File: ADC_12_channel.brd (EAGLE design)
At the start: 160 x 122.4 mm, 165 parts, among them K1 691131710003, K2 691101710002, K3 691101710002, K4 691101710002, K5 691101710002, K6 691101710002, K7 691101710002, K8 691101710002, K9 691101710002, U1 AD7864ASZ-1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

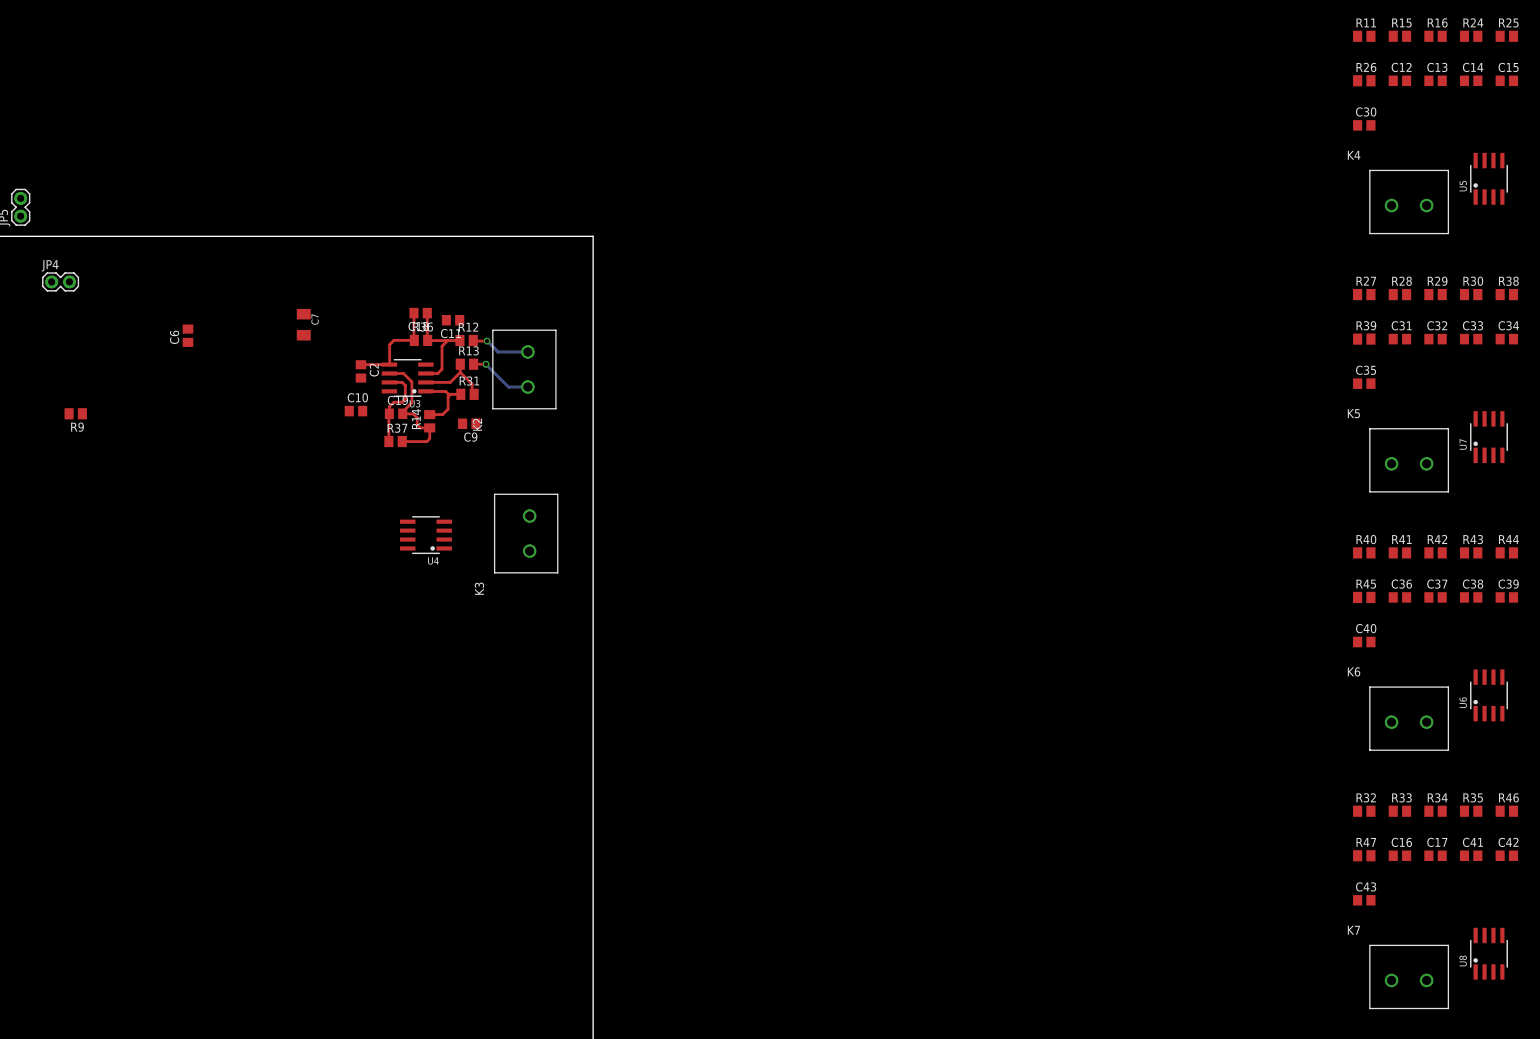
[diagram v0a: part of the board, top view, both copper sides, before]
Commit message: Routed 4 OpAmp stages for 1st ADC chip
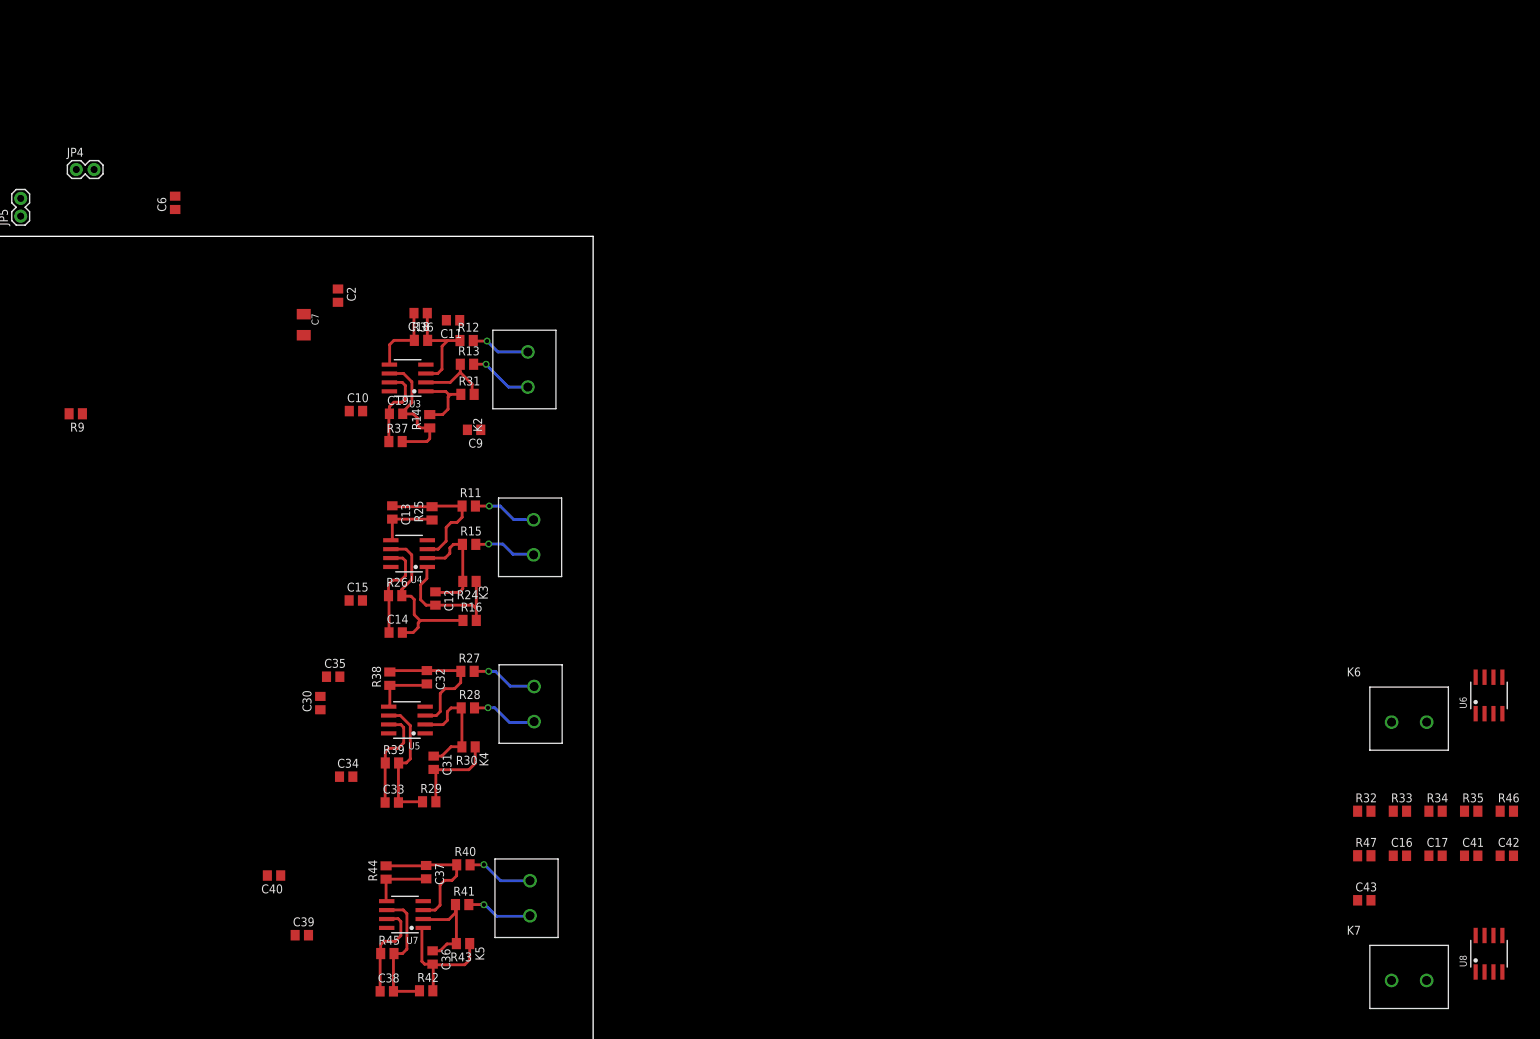
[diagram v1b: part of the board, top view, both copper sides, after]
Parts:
- moved C15 180.1 mm to (126.2, 48.1)
- moved C39 178.4 mm to (118.5, 0.36)
- moved C34 176.8 mm to (124.8, 23.0)
- moved U5 172.5 mm to (133.5, 31.0), turned to 90 degrees
- moved C14 172.3 mm to (131.9, 43.5)
- moved C30 170.1 mm to (121.1, 33.5), turned to 90 degrees
- moved U7 168.9 mm to (133.2, 3.30), turned to 90 degrees
- moved R38 168.4 mm to (131.0, 36.9), turned to 90 degrees
- moved R25 167.7 mm to (137.0, 60.5), turned to 90 degrees
- moved C33 167.5 mm to (131.3, 19.3)
- moved R44 166.2 mm to (130.5, 9.30), turned to 90 degrees
- moved C38 164.5 mm to (130.6, -7.65)
- moved R24 162.6 mm to (142.4, 50.8), turned to 180 degrees
- moved C13 161.0 mm to (131.4, 60.6), turned to 270 degrees
- moved R16 160.9 mm to (142.4, 45.2)
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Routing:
- net N$46: track 0.00 -> 24.9 mm
- net AGND: track 66.3 -> 88.5 mm
- net N$60: track 0.00 -> 20.4 mm
- net N$70: track 0.00 -> 20.2 mm
- net N$45: track 0.00 -> 19.6 mm
- net N$65: track 0.00 -> 19.5 mm
- net N$71: track 0.00 -> 19.4 mm
- net N$34: track 0.00 -> 19.1 mm
- net N$69: track 0.00 -> 18.2 mm
- net N$58: track 0.00 -> 17.1 mm
- net N$33: track 0.00 -> 16.8 mm
- net N$68: track 0.00 -> 15.6 mm
- net ADC3: track 0.00 -> 14.9 mm
- net ADC4: track 0.00 -> 14.3 mm
- net ADC2: track 0.00 -> 14.2 mm
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
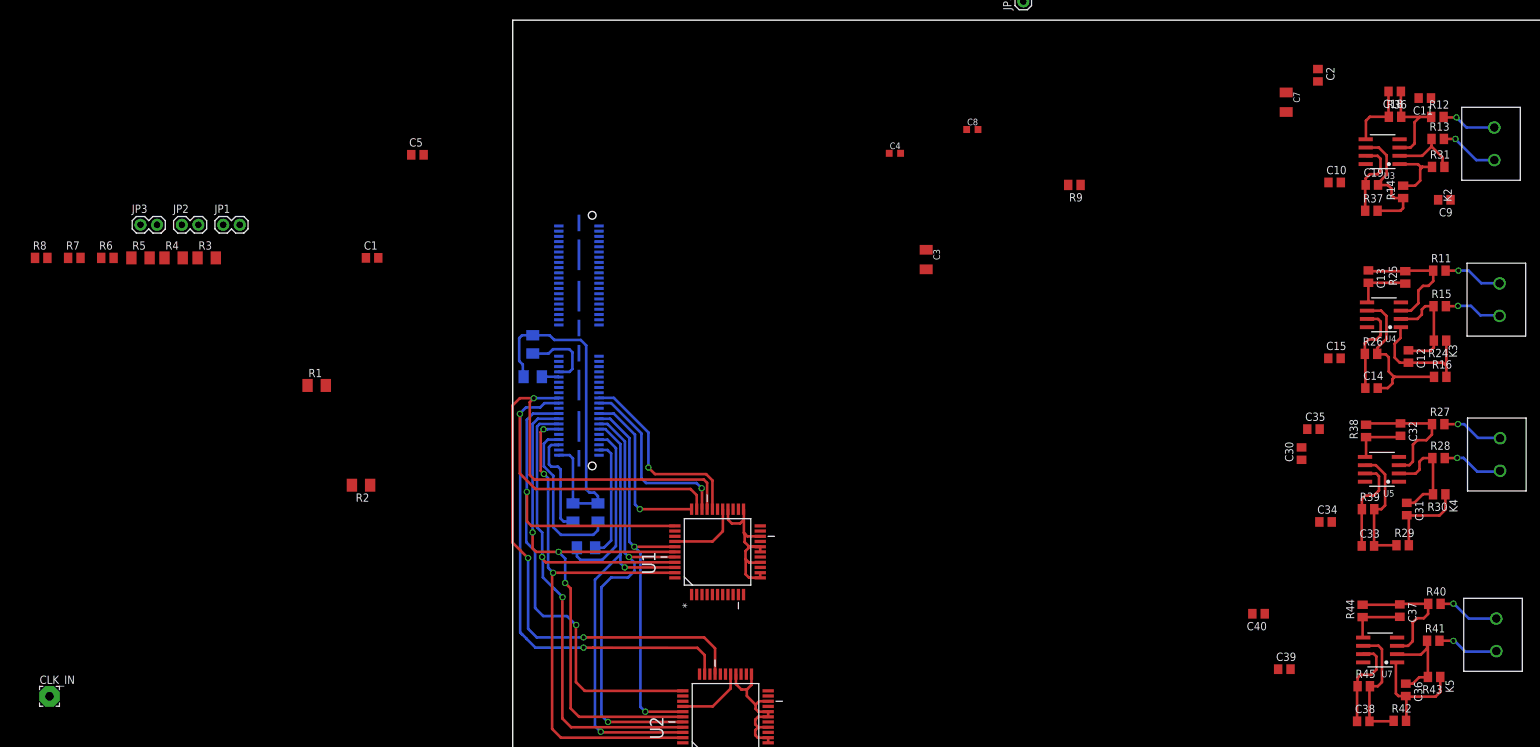
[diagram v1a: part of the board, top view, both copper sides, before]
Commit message: Added CLK INT/EXT resistor & relocated inout Opamp
Reducing the size
created possibility to input external clock
relocated the Omapms to reduce the board size.
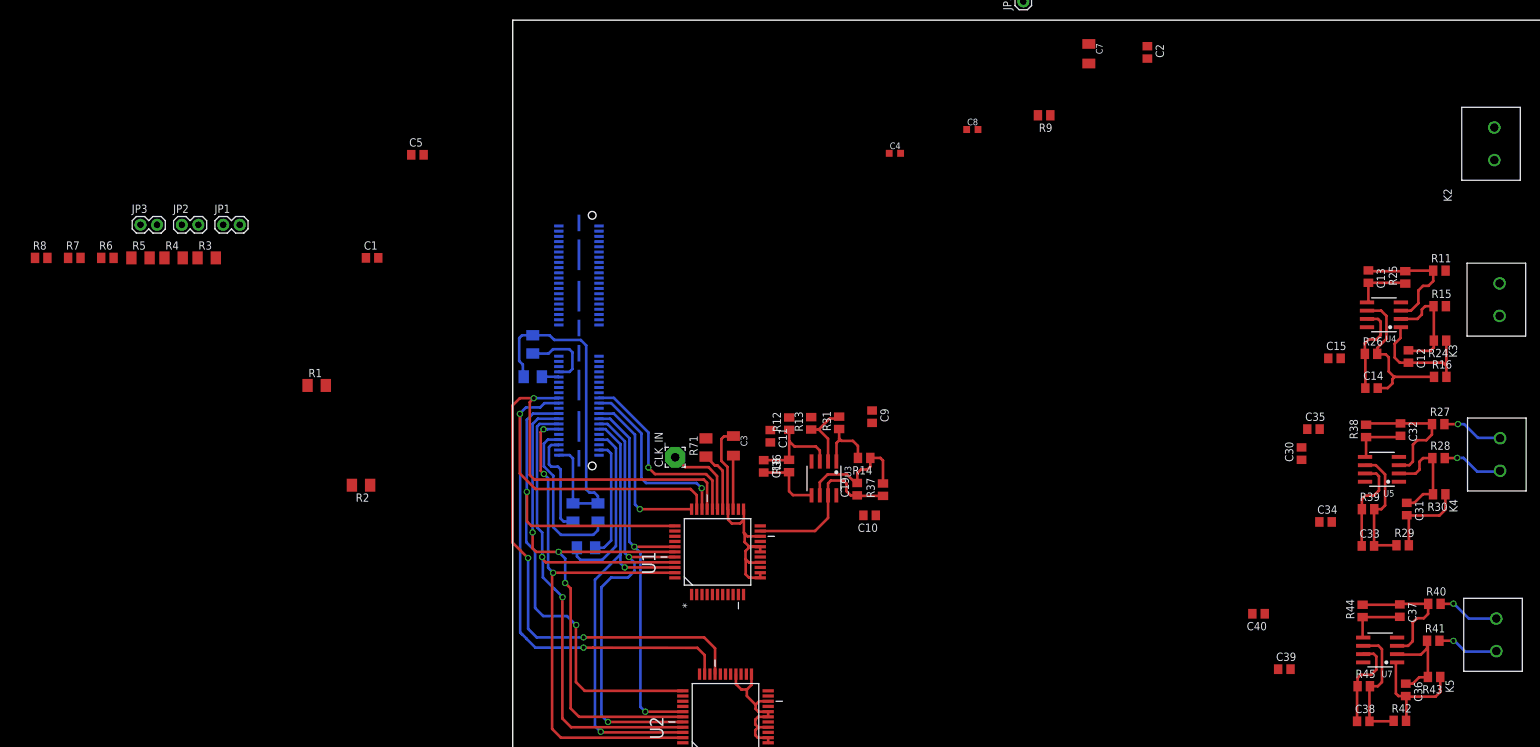
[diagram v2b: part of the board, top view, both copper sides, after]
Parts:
- added R71: 0, resistor:M1206
- moved C11 113.1 mm to (39.5, 36.1), turned to 270 degrees
- moved C18 112.7 mm to (38.5, 31.5), turned to 270 degrees
- moved R12 110.1 mm to (42.4, 38.0), turned to 90 degrees
- moved R36 107.4 mm to (42.4, 31.5), turned to 90 degrees
- moved R13 105.6 mm to (45.8, 38.1), turned to 90 degrees
- moved CLK_IN 102.8 mm to (24.9, 32.9), turned to 90 degrees
- moved R31 100.0 mm to (50.1, 38.2), turned to 90 degrees
- moved U3 99.4 mm to (47.8, 29.6), turned to 180 degrees
- moved C9 94.0 mm to (55.2, 39.1), turned to 270 degrees
- moved R14 92.3 mm to (53.9, 32.8), turned to 180 degrees
- moved C19 91.8 mm to (52.9, 28.0), turned to 90 degrees
- moved C10 87.8 mm to (54.8, 24.0), turned to 180 degrees
- moved R37 86.3 mm to (56.8, 27.9), turned to 90 degrees
- moved C3 41.2 mm to (33.9, 34.6)
- moved C7 31.2 mm to (88.4, 94.8)
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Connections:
- new net N$47: R71.1, U1.27
- net DGND: now also R71.2; no longer U1.27
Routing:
- net DGND: track 22.1 -> 0.00 mm
- net ADC1: track 12.1 -> 26.8 mm
- net AGND: track 88.5 -> 101.7 mm
- net N$11: track 0.00 -> 12.8 mm
- net N$47: track 0.00 -> 9.38 mm
- net N$32: track 9.11 -> 0.00 mm, vias 1 -> 0
- net N$28: track 9.11 -> 0.00 mm, vias 1 -> 0
- net N$31: track 8.91 -> 0.00 mm, vias 1 -> 0
- net N$54: track 8.46 -> 0.00 mm, vias 1 -> 0
- net VDD: track 0.00 -> 8.25 mm

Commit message: Removed unnecessary component Adjusted the location of ADC opamps Realigned Processors!! Very criticall
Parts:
- removed JP4: (no value), SparkFun-Retired:1X02
- removed PAD2, PAD3: WIREPAD1,6/0,8, wirepad:1,6/0,8
- added R72: 0, resistor:M1206
- moved CLK_IN1 221.9 mm to (16.9, 2.90)
- moved R3 120.4 mm to (58.0, 4.50)
- moved C6 118.8 mm to (42.6, 0.97), turned to 270 degrees
- moved R4 115.1 mm to (51.2, 12.8)
- moved C7 108.4 mm to (34.6, 0.76)
- moved R1 100.0 mm to (58.4, -2.57)
- moved R11 98.0 mm to (44.3, 58.9), turned to 90 degrees
- moved R40 93.6 mm to (51.8, 37.3), turned to 90 degrees
- moved R15 92.6 mm to (49.7, 59.0), turned to 90 degrees
- moved R25 92.0 mm to (45.3, 53.7), turned to 180 degrees
- moved C2 90.1 mm to (82.7, 6.12)
- moved R41 89.9 mm to (57.5, 37.2), turned to 90 degrees
- moved C8 88.7 mm to (37.6, 0.89), turned to 270 degrees
- moved R24 87.7 mm to (55.0, 59.0), turned to 270 degrees
- moved R43 87.2 mm to (63.0, 37.3), turned to 270 degrees
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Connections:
- net DGND: now also R72.2; no longer JP4.1
- net N$25: now also R72.1; no longer JP4.2
- net VCC_12+: no longer PAD2.1
- net VCC_12-: no longer PAD3.1
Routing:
- net ADC3: track 14.9 -> 78.4 mm
- net N$12: track 30.2 -> 77.9 mm, vias 1 -> 2
- net N$30: track 28.5 -> 73.4 mm, vias 1 -> 2
- net N$10: track 26.6 -> 67.8 mm, vias 1 -> 2
- net ADC2: track 14.2 -> 49.8 mm
- net ADC1: track 26.8 -> 55.4 mm
- net ADC4: track 14.3 -> 39.2 mm
- net N$48: track 0.00 -> 17.5 mm
- net N$66: track 9.51 -> 0.00 mm, vias 1 -> 0
- net N$67: track 9.45 -> 0.00 mm, vias 1 -> 0
- net N$53: track 9.44 -> 0.00 mm, vias 1 -> 0
- net N$57: track 9.44 -> 0.00 mm, vias 1 -> 0
- net N$7: track 120.6 -> 129.2 mm
- net N$27: track 73.0 -> 81.2 mm
- net N$9: track 60.9 -> 69.1 mm
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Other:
- board size 160 x 122.4 mm -> 160 x 127 mm

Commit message: Removed Isolating 0 ohm resistors..
End of session commit
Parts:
- removed R71: 0, resistor:M1206
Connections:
- removed net N$47: R71.1, U1.27
- net DGND: now also U1.27; no longer R71.2
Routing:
- net N$47: track 9.38 -> 0.00 mm
- net N$48: track 17.5 -> 21.2 mm
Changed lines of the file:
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@@
 <element name="CONVST" library="wirepad" package="3,17/1,3" value="" x="-145.0594" y="-199.8726"/>
 <element name="R20" library="resistor" package="M1206" value="0" x="-144.5768" y="-204.5462"/>
-<element name="R71" library="resistor" package="M1206" value="0" x="33.2486" y="34.3916" rot="R90"/>
 <element name="R72" library="resistor" package="M1206" value="0" x="30.9118" y="-24.384" rot="R270"/>
 </elements>
@@
 <wire x1="24.4602" y1="1.905" x2="29.464" y2="1.905" width="0.4064" layer="1"/>
 <wire x1="29.464" y1="1.905" x2="32.639" y2="-1.27" width="0.4064" layer="1"/>
-<wire x1="32.639" y1="-1.27" x2="32.6644" y2="-5.0038" width="0" layer="19" extent="1-16"/>
+<wire x1="32.639" y1="-1.27" x2="32.639" y2="-4.9784" width="0.4064" layer="1"/>
+<wire x1="32.639" y1="-4.9784" x2="32.6644" y2="-5.0038" width="0.4064" layer="1"/>
 </signal>
 <signal name="N$50">
@@
 <contactref element="C35" pad="2"/>
 <contactref element="C34" pad="1"/>
-<contactref element="R71" pad="2"/>
 <contactref element="R72" pad="2"/>
+<contactref element="U1" pad="27"/>
 <wire x1="289.3212" y1="-25.146" x2="270.9012" y2="-31.496" width="0" layer="19" extent="1-1"/>
 <wire x1="289.3212" y1="-61.976" x2="270.9012" y2="-31.496" width="0" layer="19" extent="1-1"/>
@@
 <wire x1="38.8112" y1="60.0812" x2="65.7098" y2="53.152" width="0" layer="19" extent="1-1"/>
 <wire x1="27.62" y1="43.8912" x2="38.8112" y2="60.0812" width="0" layer="19" extent="1-1"/>
-<wire x1="33.2486" y1="35.7916" x2="27.62" y2="43.8912" width="0" layer="19" extent="1-1"/>
-<wire x1="28.4734" y1="19.9644" x2="33.2486" y2="35.7916" width="0" layer="19" extent="1-1"/>
+<wire x1="35.814" y1="24.9174" x2="27.62" y2="43.8912" width="0" layer="19" extent="1-1"/>
+<wire x1="28.4734" y1="19.9644" x2="35.814" y2="24.9174" width="0" layer="19" extent="1-1"/>
 <wire x1="33.4518" y1="-5.0038" x2="28.4734" y2="19.9644" width="0" layer="19" extent="1-1"/>
 <wire x1="26.1112" y1="-9.9568" x2="33.4518" y2="-5.0038" width="0" layer="19" extent="1-1"/>
+<wire x1="30.9118" y1="-25.784" x2="26.1112" y2="-9.9568" width="0" layer="19" extent="1-1"/>
 <wire x1="-22.54" y1="63.5" x2="27.62" y2="43.8912" width="0" layer="19" extent="1-1"/>
 <wire x1="-15.5804" y1="79.3242" x2="-22.54" y2="63.5" width="0" layer="19" extent="1-1"/>
 <wire x1="-50.8" y1="68.58" x2="-22.54" y2="63.5" width="0" layer="19" extent="1-1"/>
-<wire x1="30.9118" y1="-25.784" x2="26.1112" y2="-9.9568" width="0" layer="19" extent="1-1"/>
 </signal>
 <signal name="AGND">
@@
 <wire x1="-145.0594" y1="-199.8726" x2="-143.1768" y2="-204.5462" width="0" layer="19" extent="1-1"/>
 </signal>
-<signal name="N$47">
-<contactref element="R71" pad="1"/>
-<contactref element="U1" pad="27"/>
-<wire x1="35.814" y1="24.9174" x2="35.814" y2="30.8356" width="0.4064" layer="1"/>
-<wire x1="35.814" y1="30.8356" x2="35.0012" y2="31.6484" width="0.4064" layer="1"/>
-<wire x1="35.0012" y1="31.6484" x2="34.5918" y2="31.6484" width="0.4064" layer="1"/>
-<wire x1="34.5918" y1="31.6484" x2="33.2486" y2="32.9916" width="0.4064" layer="1"/>
-</signal>
 </signals>
